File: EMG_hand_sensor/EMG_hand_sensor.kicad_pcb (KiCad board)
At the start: 4 copper layers, 73.9 x 41.5 mm, 50 parts, among them J1 USB_C_Receptacle_USB2.0_16P, J2 Conn_01x04_Pin, J4 AudioJack3, J5 AudioJack3, J6 AudioJack3, SW1 SW_SPDT, U1 USBLC6-2SC6, U2 STM32F103C8T6, U3 INA333xxDGK, U4 INA333xxDGK, U5 INA333xxDGK, U7 LT1762, Y1 16MHz

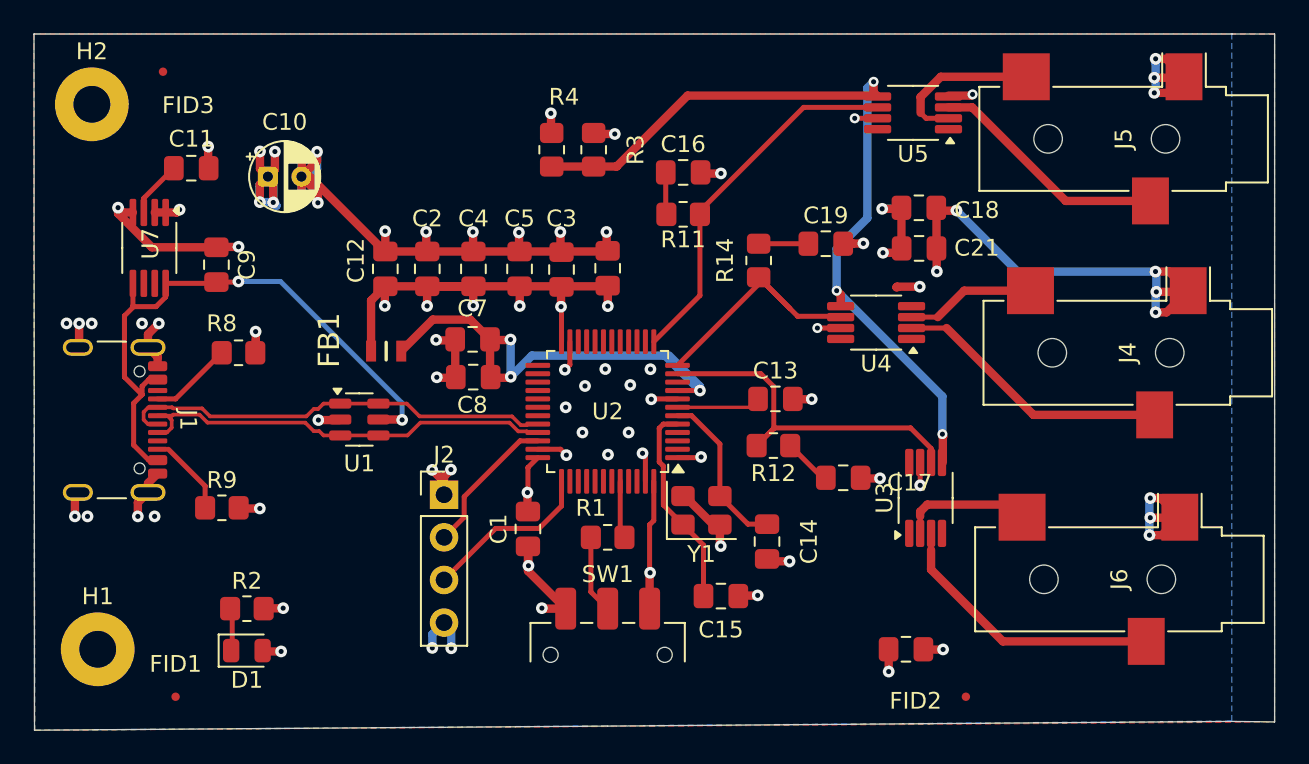
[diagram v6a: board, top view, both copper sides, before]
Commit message: ordered boards from jlcpcb
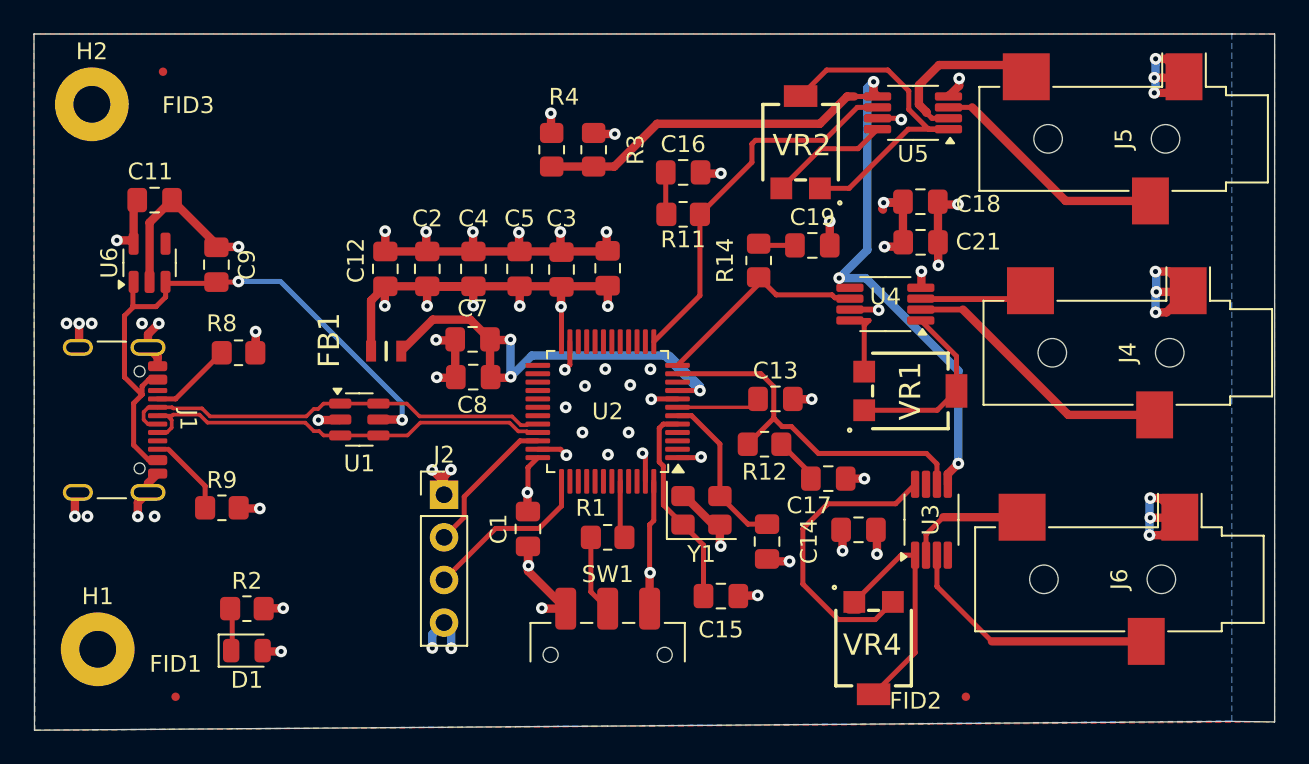
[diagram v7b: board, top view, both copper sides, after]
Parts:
- removed C10: 10uF, Capacitor_THT:CP_Radial_D4.0mm_P2.00mm
- removed U7: LT1762, Package_SO:MSOP-8_3x3mm_P0.65mm
- added U6: MIC5504-3.3YM5, Package_TO_SOT_SMD:SOT-23-5, F.Cu at (150.7, 63.6)
- added VR1: 3314G-1-101E, Bourne_pot_smd:3314G-1, F.Cu at (196.0, 71.3)
- added VR2: 3314G-1-101E, Bourne_pot_smd:3314G-1, F.Cu at (189.5, 56.5)
- added VR4: 3314G-1-101E, Bourne_pot_smd:3314G-1, F.Cu at (193.8, 86.6)
- C11: value 10nF -> 1uF
- moved C20 7.66 mm to (192.9, 79.5)
- moved C11 2.89 mm to (151.0, 59.9), turned to 0 degrees
- moved U3 1.35 mm to (197.3, 79.0)
- moved U4 1.23 mm to (194.6, 66.1)
- moved C17 0.89 mm to (191.2, 76.5)
- moved C19 0.81 mm to (190.2, 62.6)
- moved R12 0.54 mm to (187.3, 74.5)
- moved C21 0.37 mm to (196.7, 62.4)
- moved C18 0.37 mm to (196.6, 60.0)
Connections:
- C11 pad 2: Net-(U7-BYP) -> GND
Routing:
- net GND: track 149.3 -> 115.7 mm, vias 65 -> 60
- net Net-(VR2-CCW): track 0.00 -> 20.7 mm
- net Net-(VR4-CW): track 0.00 -> 17.8 mm
- net Net-(VR4-CCW): track 0.00 -> 14.7 mm
- net +3.3V: track 76.7 -> 65.6 mm, vias 25 -> 19
- net Net-(VR1-CCW): track 0.00 -> 11.1 mm
- net Net-(VR2-CW): track 0.00 -> 7.20 mm
- net Net-(VR1-CW): track 0.00 -> 4.31 mm
- net Net-(U7-BYP): track 3.38 -> 0.00 mm
- net /O3: track 15.8 -> 13.2 mm
- net +1V6: track 49.2 -> 51.6 mm
- net /E6: track 11.0 -> 13.3 mm
- net /E5: track 17.4 -> 15.8 mm
- net /E2: track 10.5 -> 11.5 mm
- net Net-(C19-Pad1): track 2.96 -> 2.20 mm
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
